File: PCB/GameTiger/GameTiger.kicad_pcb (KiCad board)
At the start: 2 copper layers, 81.3 x 99.8 mm, 71 parts, among them J1 USB TypeC Connector, J2 503398-1892, J3 LCD Display, J4 Speaker, Q1 DMG3415, U1 RP2040, U2 MCP73831-2-OT, U3 W25Q64JVSSIQ, U4 PAM8302A, U5 AP2112K-3.3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

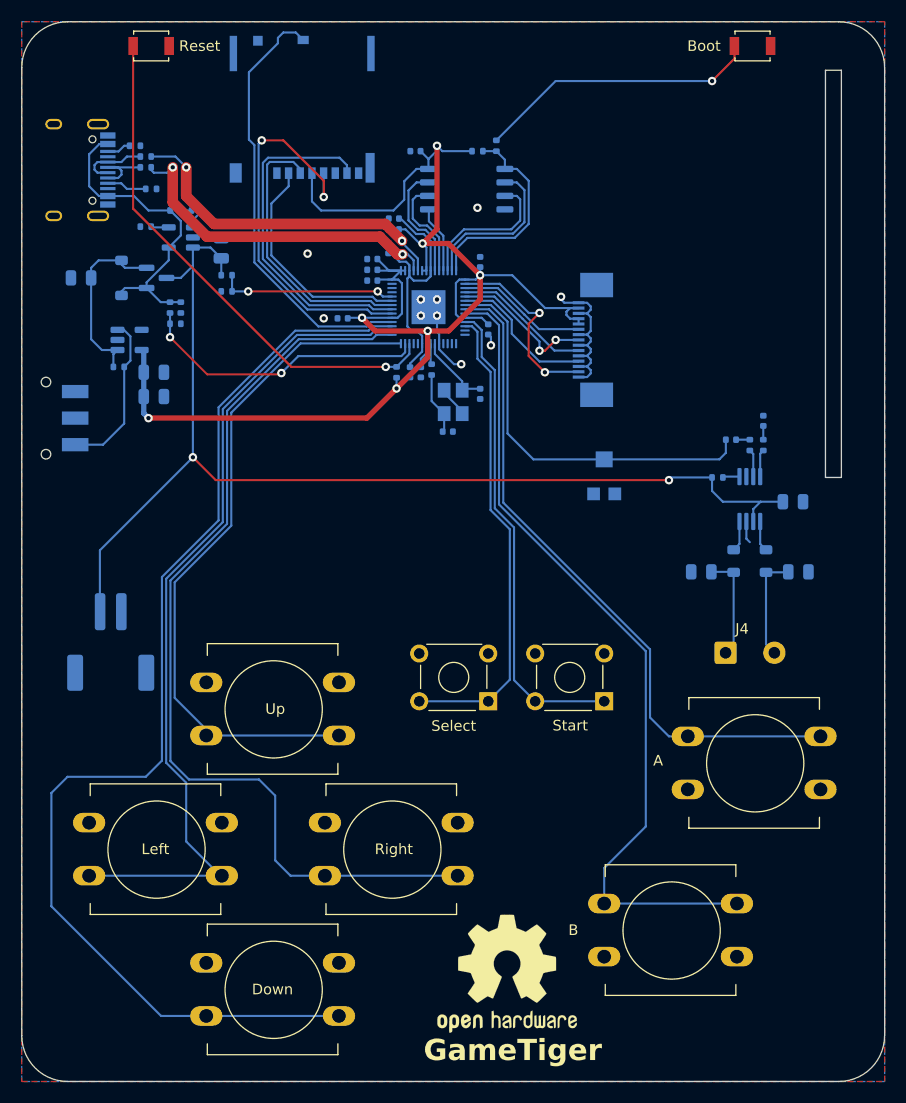
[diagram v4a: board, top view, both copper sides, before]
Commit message: Added reference link for PCB design, fixed differential pair routes and uncut GND plane on the other side
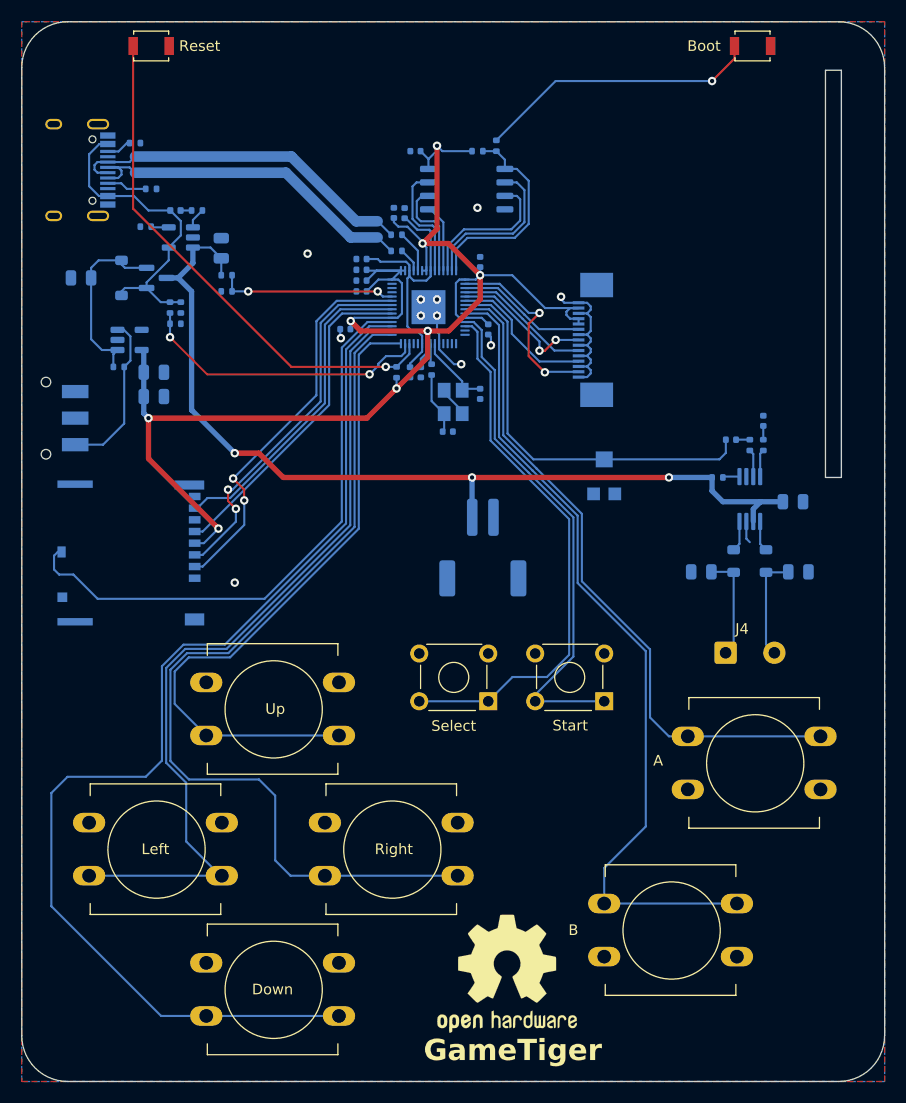
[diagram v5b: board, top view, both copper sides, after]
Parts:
- moved J2 44.3 mm to (46.2, 85.9), turned to 90 degrees
- moved X1 36.2 mm to (79.0, 85.3)
- moved R4 24.9 mm to (70.9, 57.4)
- moved R3 24.7 mm to (70.9, 55.9)
- moved C9 2.74 mm to (67.6, 58.2), turned to 180 degrees
- moved C15 1.55 mm to (70.6, 53.8), turned to 90 degrees
- moved C12 1.44 mm to (67.6, 59.2)
- moved C16 1.44 mm to (67.6, 61.2)
- moved C6 1.44 mm to (67.6, 60.2)
- moved C13 1.14 mm to (71.6, 53.8), turned to 90 degrees
- moved C8 1.05 mm to (66.0, 64.8)
- moved R21 0.25 mm to (46.2, 47.2)
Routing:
- net Net-(U1-USB_DM): track 31.8 -> 2.31 mm, vias 2 -> 0
- net Net-(U1-USB_DP): track 31.9 -> 4.00 mm, vias 2 -> 0
- net POWER_USB_DN: track 6.27 -> 33.2 mm
- net POWER_USB_DP: track 6.46 -> 33.1 mm
- net VBAT: track 105.8 -> 88.1 mm, vias 2 -> 3
- net MicroSD_CS: track 21.6 -> 37.1 mm, vias 0 -> 2
- net MicroSD_DETECT: track 41.0 -> 55.5 mm
- net MicroSD_MOSI: track 25.8 -> 35.5 mm, vias 0 -> 2
- net KYBD_SELECT: track 44.8 -> 51.3 mm
- net MicroSD_CLK: track 37.3 -> 31.4 mm, vias 2 -> 0
- net +3.3V: track 144.5 -> 150.0 mm, vias 7 -> 8
- net KYBD_START: track 45.4 -> 48.4 mm
- net +1V1: track 22.8 -> 24.9 mm
- net MicroSD_MISO: track 32.3 -> 30.7 mm
- net KYBD_UP: track 65.0 -> 63.5 mm
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
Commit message: Minor fixes in PCB design
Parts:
- added FID1: ~, Fiducial:Fiducial_1mm_Mask2mm, F.Cu at (40.9, 130.3)
- added FID2: ~, Fiducial:Fiducial_1mm_Mask2mm, F.Cu at (111.5, 130.3)
- added FID3: ~, Fiducial:Fiducial_1mm_Mask2mm, F.Cu at (40.9, 41.1)
- moved C2 3.45 mm to (75.9, 68.8), turned to 0 degrees
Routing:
- net Crystal_XIN: track 7.00 -> 5.82 mm
- net GND: track 28.7 -> 28.4 mm, vias 11 -> 16

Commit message: PCB design completed and ordered for fab
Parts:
- removed FID1, FID2, FID3: ~, Fiducial:Fiducial_1mm_Mask2mm
- added J5: Conn_01x03, Connector_Wire:SolderWire-0.25sqmm_1x03_P4.2mm_D0.65mm_OD1.7mm, F.Cu at (40.4, 104.1)
- Power1: footprint Button_Switch_SMD:SW_SPDT_CK-JS102011SAQN -> MK-12C02-G020:MK-12C02-G020_GSW
- U5: footprint Package_TO_SOT_SMD:SOT-23-5 -> AP2112K-3-3TRG1:SOT_RG1_DIO
- moved C3 2.96 mm to (74.2, 71.9), turned to 90 degrees
- moved J2 2.79 mm to (43.4, 85.9), turned to -90 degrees
- moved C2 1.85 mm to (77.7, 69.3), turned to 180 degrees
- moved R5 1.30 mm to (75.4, 68.8)
- moved Power1 1.05 mm to (37.6, 72.1)
- moved C7 0.80 mm to (73.9, 69.1)
- moved Y1 0.76 mm to (77.0, 71.6), turned to 180 degrees
- moved C11 0.72 mm to (72.6, 69.3)
- moved C8 0.51 mm to (66.0, 65.3)
- moved R16 0.25 mm to (70.6, 68.8)
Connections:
- Power1 pad 3: (no net) -> unconnected-(Power1-Pad3)
- U1 pad 24: unconnected-(U1-SWCLK-Pad24) -> SW_CLK
- U1 pad 25: unconnected-(U1-SWD-Pad25) -> SW_DIO
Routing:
- net SW_CLK: track 0.00 -> 58.7 mm, vias 0 -> 1
- net SW_DIO: track 0.00 -> 51.4 mm, vias 0 -> 1
- net MicroSD_DETECT: track 55.5 -> 31.8 mm
- net MicroSD_MISO: track 30.7 -> 49.5 mm, vias 0 -> 2
- net MicroSD_CLK: track 31.4 -> 47.8 mm, vias 0 -> 2
- net MicroSD_MOSI: track 35.5 -> 50.4 mm, vias 2 -> 0
- net MicroSD_CS: track 37.1 -> 49.8 mm, vias 2 -> 0
- net +3.3V: track 150.0 -> 153.3 mm
- net KYBD_DOWN: track 107.1 -> 104.2 mm
- net KYBD_LEFT: track 78.4 -> 75.4 mm
- net KYBD_RIGHT: track 87.2 -> 84.3 mm
- net KYBD_UP: track 63.5 -> 60.5 mm
- net Crystal_XIN: track 5.82 -> 8.52 mm
- net GND: track 28.4 -> 26.2 mm, vias 16 -> 15
- net Crystal_XOUT: track 5.68 -> 3.56 mm
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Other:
- board text added: "v3.0"
- board text removed: "+"

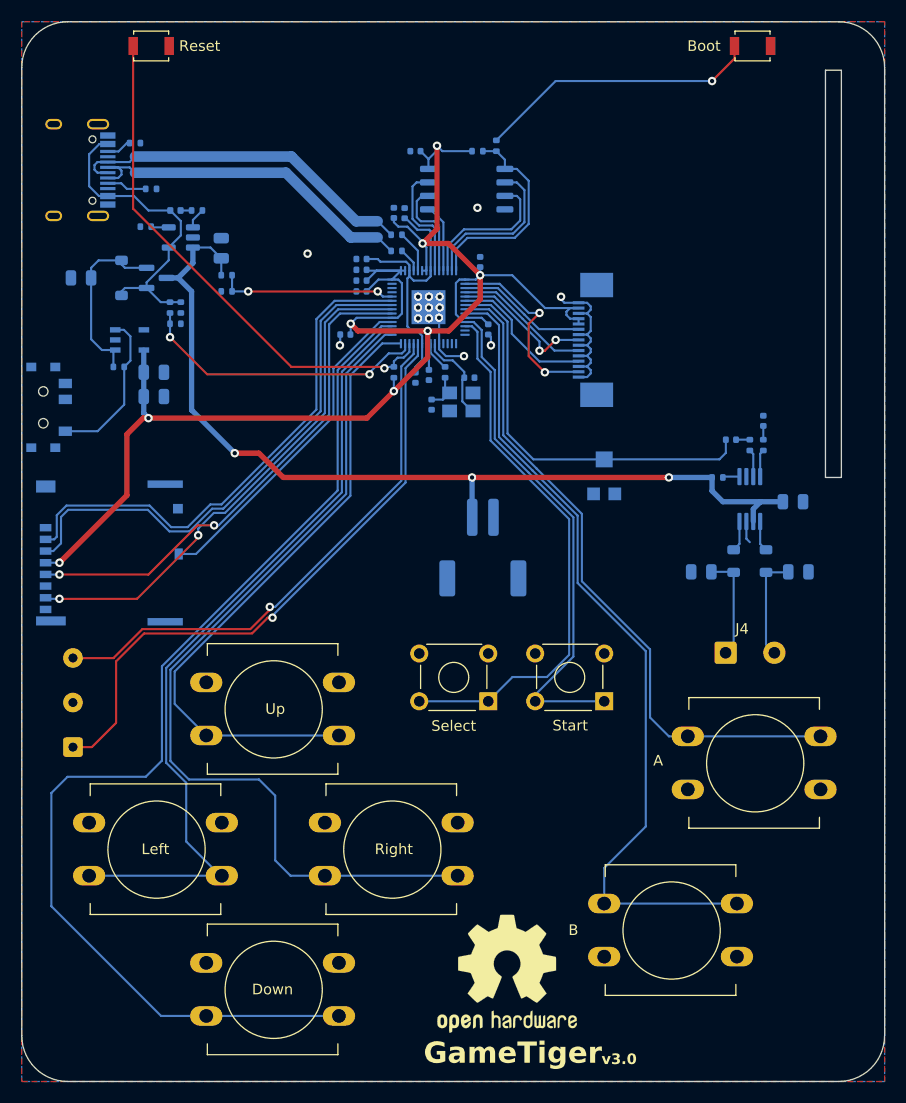
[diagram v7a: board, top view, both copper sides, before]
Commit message: Added Blender file for 3D printing Case
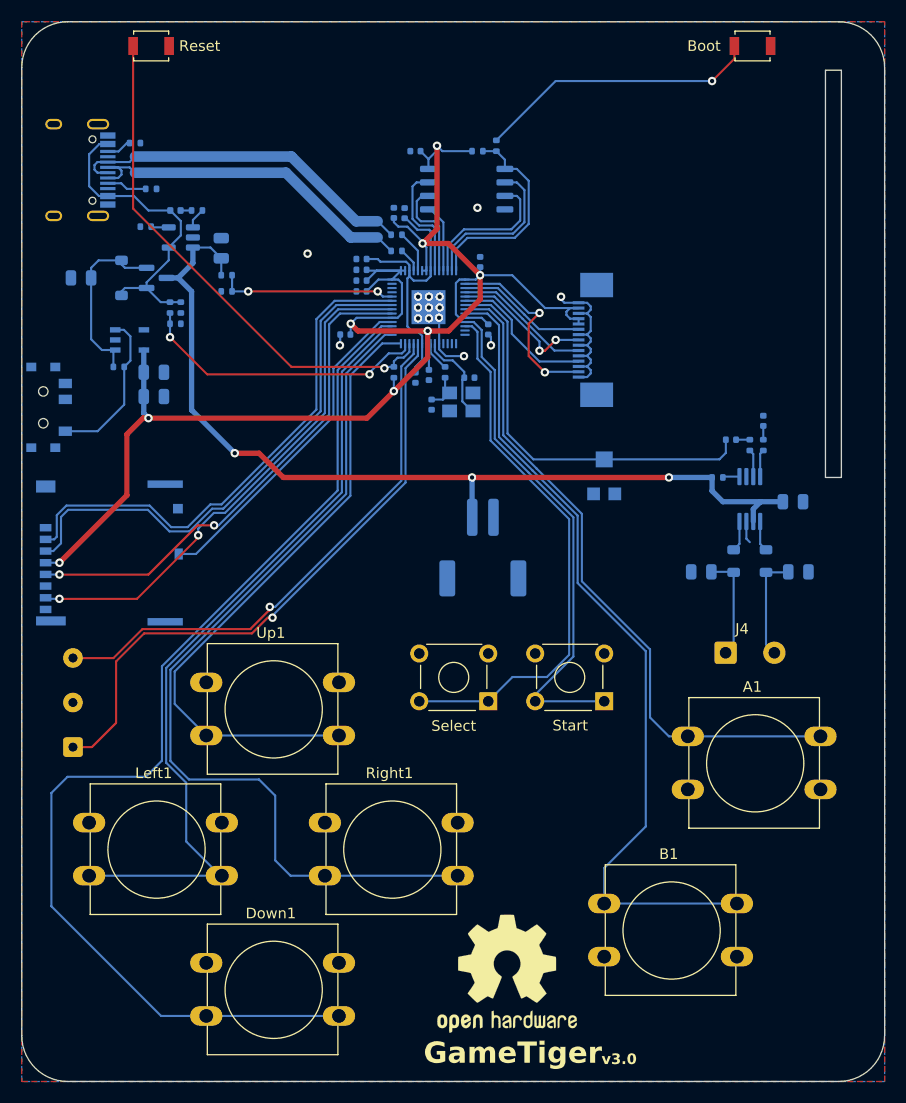
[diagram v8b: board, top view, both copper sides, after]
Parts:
- A1, B1, Down1, Left1, Right1, Up1: footprint Button_Switch_THT:SW_PUSH-12mm -> Button_Switch_THT:SW_PUSH-12mm_3DModel
